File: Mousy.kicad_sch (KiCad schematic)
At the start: 4 parts, among them J1 Mouse_out, J2 Mouse_in, U1 74LS125

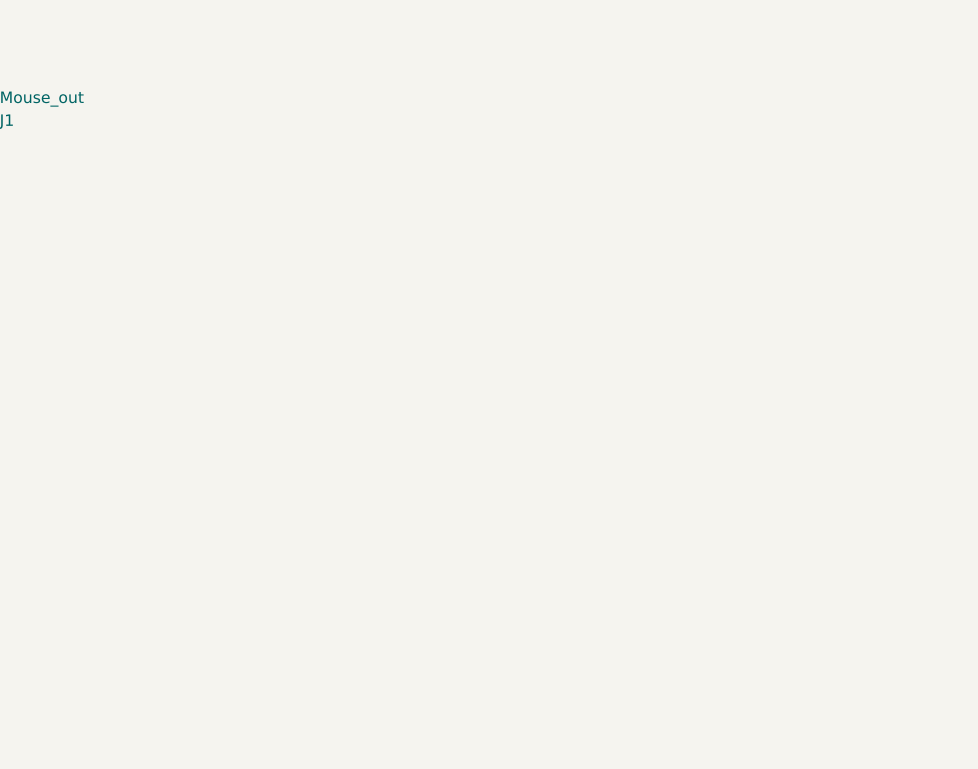
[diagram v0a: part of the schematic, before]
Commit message: add mouse, fix some gnd nets
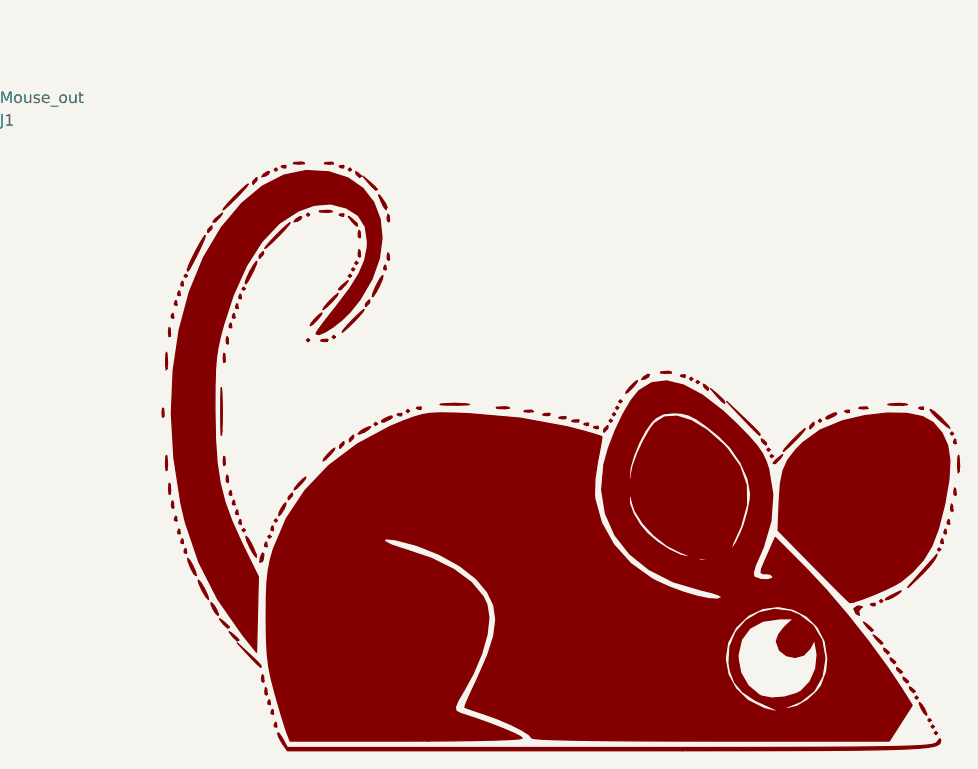
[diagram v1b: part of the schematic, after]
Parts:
- added Logo1: Mouse-, localfootprints:Mouse+, symbol logos:Mouse-
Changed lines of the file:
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@@
+    )
+  )
+  (symbol (lib_id "logos:Mouse-") (at 231.775 121.92 0) (unit 1)
+    (in_bom yes) (on_board yes) (dnp no) (fields_autoplaced)
+    (property "Reference" "Logo1" (at 231.775 88.9268 0)
+      (effects (font (size 1.27 1.27)) hide)
+    )
+    (property "Value" "Mouse-" (at 231.775 154.9132 0)
+      (effects (font (size 1.27 1.27)) hide)
+    )
+    (property "Footprint" "localfootprints:Mouse+" (at 231.775 121.92 0)
+      (effects (font (size 1.27 1.27)) hide)
+    )
+    (property "Datasheet" "" (at 231.775 121.92 0)
+      (effects (font (size 1.27 1.27)) hide)
+    )
+    (instances
+      (project "Mousy"
+        (path "/01dbafac-20eb-4fe2-9d33-d04ff2f6a8b1"
+          (reference "Logo1") (unit 1)
+        )
+      )
     )
   )
